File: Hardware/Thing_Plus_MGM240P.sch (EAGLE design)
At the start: 54 parts, among them J1 THING_PLUS_LOGICAL, J2 USB Female Type C Connector, J3 QWIIC_RIGHT_ANGLE, J5 MICRO-SDFRICTION, Q1 20V/4.2A/52mΩ/1.4W, U1 MGM240P, U2 3.3V, U4 MCP73831, U5 MAX17048, U6 MK22FN128VLH10

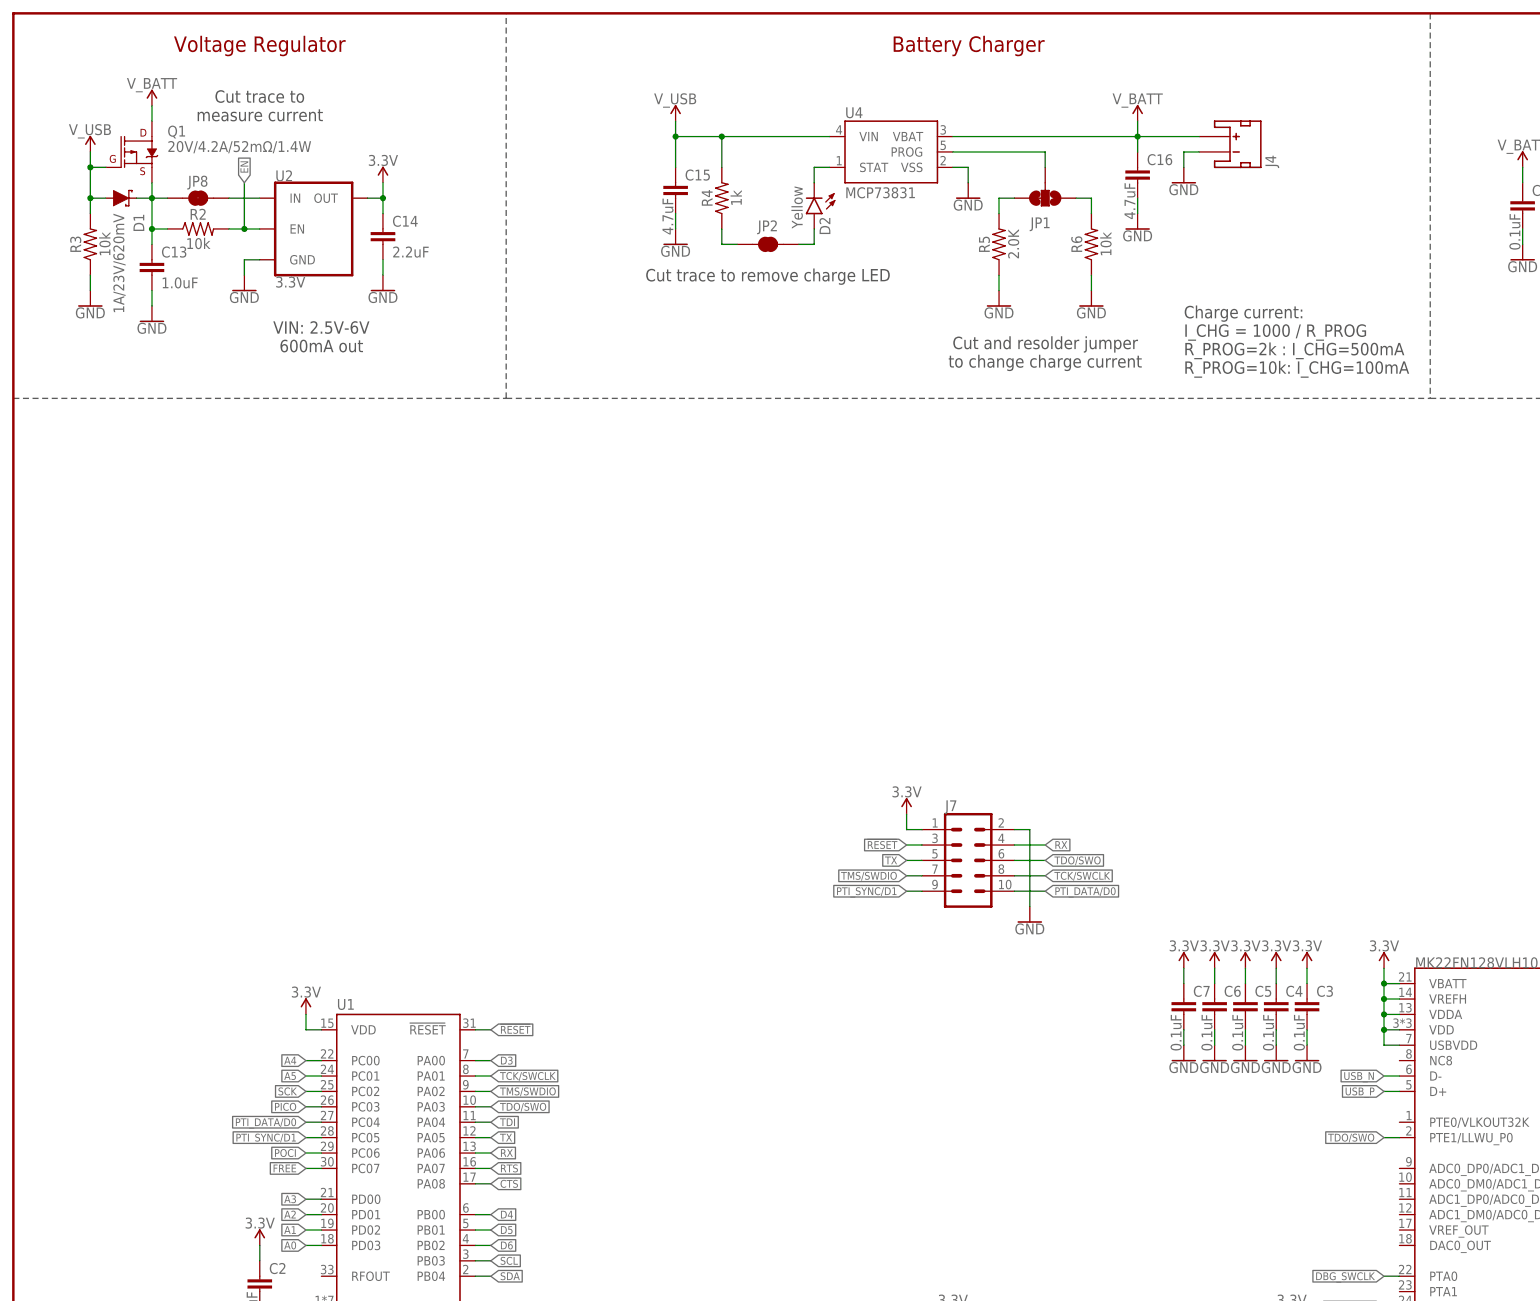
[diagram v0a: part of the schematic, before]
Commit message: Schematic and board updates
Disconnect RTS and CTS pins
Add status LED
Complete more of the routing and component placement
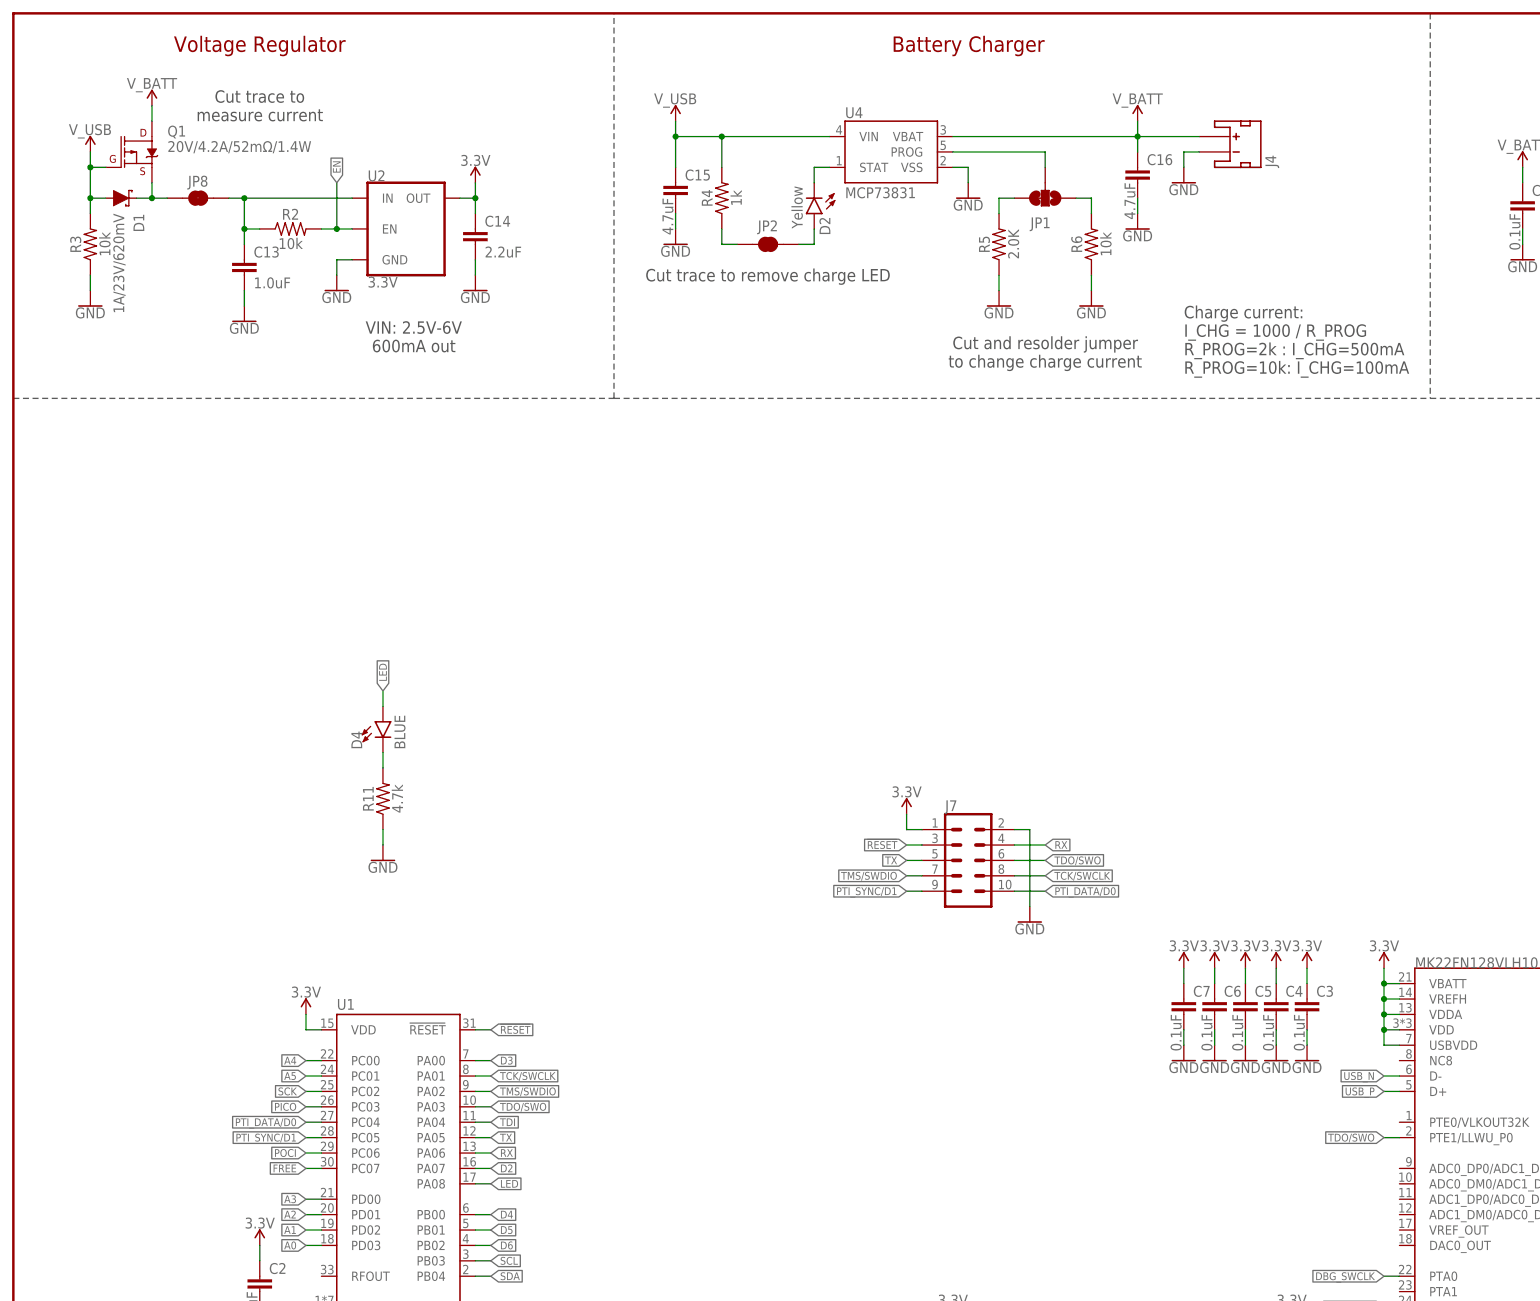
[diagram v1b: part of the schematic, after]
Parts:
- added D4: BLUE, SparkFun-LED:LED-BLUE0603
- added R11: 4.7k, SparkFun-Resistors:4.7KOHM-0402T-1/16W-1%
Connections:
- removed net N$2: C13.1, D1.C, JP8.1, Q1.S, R2.1
- new net LED: D4.A, U1.PA08
- new net N$1: D4.C, R11.2
- new net N$7: D1.C, JP8.1, Q1.S
- net CTS: no longer U1.PA08
- net D2: now also U1.PA07
- net GND: now also R11.1
- net N$27: now also C13.1, R2.1
- net RTS: no longer U1.PA07
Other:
- moved on the sheet: C13, C14, R2, U2

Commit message: Finalize initial schematic and board
Clean up schematic and finalize nets
Finish routing board (needs improved GND continuity
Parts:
- added LOGO1: SFE_LOGO_NAME_FLAME.1_INCH, SparkFun-Aesthetics:SFE_LOGO_NAME_FLAME.1_INCH
- added LOGO2: QWIIC_LOGO_3MM, SparkFun-Aesthetics:QWIIC_LOGO_3MM
- added LOGO3: OSHW-LOGOS, SparkFun-Aesthetics:OSHW-LOGOS
- added Q2: 20V/4.2A/52mΩ/1.4W, SparkFun-DiscreteSemi:MOSFET_PCH-DMG2305UX-7
- added R12: 100k, SparkFun-Resistors:100KOHM-0402T-1/16W-1%
- added VDDJ_EN: JUMPER-SMT_2_NO_SILK, SparkFun-Jumpers:JUMPER-SMT_2_NO_SILK
- renumbered JP2 to CHG, JP3 to I2C, JP4 to SHLD, JP8 to MEAS
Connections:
- removed net SCL1: U5.SCL
- removed net SDA1: U5.SDA
- new net !VDDJ_EN!: Q2.G, R12.2, VDDJ_EN.2
- new net VDD: C3.1, C4.1, C5.1, C6.1, C7.1, Q2.D, R1.2, TP1.1, U6.PTA4/LLWU_P3, U6.USBVDD, U6.VBATT, U6.VDD, U6.VDDA, U6.VREFH
- net 3.3V: now also Q2.S; no longer C3.1, C4.1, C5.1, C6.1, C7.1, R1.2, TP1.1, U6.PTA4/LLWU_P3, U6.USBVDD, U6.VBATT, U6.VDD, U6.VDDA, U6.VREFH
- net A0: now also VDDJ_EN.1
- net GND: now also R12.1
- net SCL: now also U5.SCL
- net SDA: now also U5.SDA
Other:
- note added: "Close jumper to enable power control of J-Link OB Debugger"
- note added: "Dryw Wade"
- note added: "J-Link 6 Pin Adapter Test Points"
- note added: "J-Link OB Debugger"
- note added: "J-Link OB Power Control"
- note added: "MGM240P"
- note added: "Mini Simplicity Connector"
- note added: "Status LED"
- note added: "Thing Plus Pinout"
- note added: "v01"
- moved on the sheet: C2, C3, C4, C5, C6, C7, D4, J1, J5, J7, R1, R11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

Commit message: Add polish
Improve GND continuity
Fix and approve DRC errors
Add SFE flame and OSHW logo to top silk
Add pin and jumper labels to bottom silk
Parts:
- renumbered JP1 to CHG_I, VDDJ_EN to VJ_CTRL
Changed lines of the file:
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@@
 <part name="R5" library="SparkFun-Resistors" deviceset="2.0KOHM" device="-0402T-1/16W-1%" value="2.0K"/>
 <part name="R6" library="SparkFun-Resistors" deviceset="10KOHM" device="-0402T-1/16W-1%" value="10k"/>
-<part name="JP1" library="SparkFun-Jumpers" deviceset="JUMPER-SMT_3_1-NC_TRACE" device="_SILK" package3d_urn="urn:adsk.eagle:package:39288/1"/>
+<part name="CHG_I" library="SparkFun-Jumpers" deviceset="JUMPER-SMT_3_1-NC_TRACE" device="_SILK" package3d_urn="urn:adsk.eagle:package:39288/1"/>
 <part name="GND29" library="SparkFun-PowerSymbols" deviceset="GND" device=""/>
 <part name="GND30" library="SparkFun-PowerSymbols" deviceset="GND" device=""/>
@@
 <part name="R12" library="SparkFun-Resistors" deviceset="100KOHM" device="-0402T-1/16W-1%" value="100k"/>
 <part name="GND18" library="SparkFun-PowerSymbols" deviceset="GND" device=""/>
-<part name="VDDJ_EN" library="SparkFun-Jumpers" deviceset="JUMPER-SMT_2_NO" device="_SILK" package3d_urn="urn:adsk.eagle:package:39279/1"/>
+<part name="VJ_CTRL" library="SparkFun-Jumpers" deviceset="JUMPER-SMT_2_NO" device="_SILK" package3d_urn="urn:adsk.eagle:package:39279/1"/>
 <part name="LOGO1" library="SparkFun-Aesthetics" deviceset="SFE_LOGO_NAME_FLAME" device=".1_INCH"/>
 <part name="LOGO2" library="SparkFun-Aesthetics" deviceset="QWIIC_LOGO" device="_3MM"/>
@@
 <attribute name="VALUE" x="179.324" y="241.3" size="1.778" layer="96" font="vector" rot="R90" align="top-center"/>
 </instance>
-<instance part="JP1" gate="G$1" x="170.18" y="248.92" smashed="yes" rot="R270">
+<instance part="CHG_I" gate="G$1" x="170.18" y="248.92" smashed="yes" rot="R270">
 <attribute name="NAME" x="169.418" y="244.856" size="1.778" layer="95" font="vector" rot="R180" align="center"/>
 </instance>
@@
 <attribute name="VALUE" x="297.18" y="169.926" size="1.778" layer="96" align="top-center"/>
 </instance>
-<instance part="VDDJ_EN" gate="G$1" x="297.18" y="162.56" smashed="yes">
+<instance part="VJ_CTRL" gate="G$1" x="297.18" y="162.56" smashed="yes">
 <attribute name="NAME" x="297.18" y="165.354" size="1.778" layer="95" font="vector" align="center"/>
 </instance>
@@
 <pinref part="R6" gate="G$1" pin="2"/>
 <wire x1="177.8" y1="246.38" x2="177.8" y2="248.92" width="0.1524" layer="91"/>
-<pinref part="JP1" gate="G$1" pin="1"/>
+<pinref part="CHG_I" gate="G$1" pin="1"/>
 <wire x1="177.8" y1="248.92" x2="175.26" y2="248.92" width="0.1524" layer="91"/>
 </segment>
@@
 <pinref part="R5" gate="G$1" pin="2"/>
 <wire x1="162.56" y1="246.38" x2="162.56" y2="248.92" width="0.1524" layer="91"/>
-<pinref part="JP1" gate="G$1" pin="3"/>
+<pinref part="CHG_I" gate="G$1" pin="3"/>
 <wire x1="162.56" y1="248.92" x2="165.1" y2="248.92" width="0.1524" layer="91"/>
 </segment>
@@
 <net name="N$9" class="0">
 <segment>
-<pinref part="JP1" gate="G$1" pin="2"/>
+<pinref part="CHG_I" gate="G$1" pin="2"/>
 <wire x1="170.18" y1="254" x2="170.18" y2="256.54" width="0.1524" layer="91"/>
 <pinref part="U4" gate="G$1" pin="PROG"/>
@@
 </segment>
 <segment>
-<pinref part="VDDJ_EN" gate="G$1" pin="1"/>
+<pinref part="VJ_CTRL" gate="G$1" pin="1"/>
 <wire x1="292.1" y1="162.56" x2="289.56" y2="162.56" width="0.1524" layer="91" style="longdash"/>
 <label x="289.56" y="162.56" size="1.27" layer="95" rot="R180" xref="yes"/>
@@
 </segment>
 <segment>
-<pinref part="VDDJ_EN" gate="G$1" pin="2"/>
+<pinref part="VJ_CTRL" gate="G$1" pin="2"/>
 <wire x1="302.26" y1="162.56" x2="304.8" y2="162.56" width="0.1524" layer="91" style="longdash"/>
 <label x="304.8" y="162.56" size="1.27" layer="95" xref="yes"/>

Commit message: Update voltage regulator
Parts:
- U2: value 3.3V -> XC6222B331MR-G; device SparkFun-IC-Power:V_REG_AP2112K-3.3V -> SparkFun-IC-Power:XC6222B331MR-G
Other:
- note added: "VIN: 2.5V-6V 700mA out"
- note removed: "VIN: 2.5V-6V 600mA out"
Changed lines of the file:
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@@
 <part name="GND5" library="SparkFun-PowerSymbols" deviceset="GND" device=""/>
 <part name="SUPPLY8" library="SparkFun-PowerSymbols" deviceset="V_BATT" device=""/>
-<part name="U2" library="SparkFun-IC-Power" deviceset="V_REG_AP2112" device="K-3.3V" value="3.3V"/>
+<part name="U2" library="SparkFun-IC-Power" deviceset="XC6222" device="B331MR-G" value="XC6222B331MR-G"/>
 <part name="SUPPLY9" library="SparkFun-PowerSymbols" deviceset="3.3V" device=""/>
 <part name="GND6" library="SparkFun-PowerSymbols" deviceset="GND" device=""/>
@@
 to change charge current</text>
 <text x="66.04" y="226.06" size="2.032" layer="97" font="vector" align="center">VIN: 2.5V-6V
-600mA out</text>
+700mA out</text>
 <text x="335.28" y="228.6" size="2.032" layer="97" font="vector" align="center">Cut trace to isolate
 shield from GND</text>
@@
 <instance part="U2" gate="G$1" x="66.04" y="243.84" smashed="yes">
 <attribute name="NAME" x="58.42" y="251.714" size="1.778" layer="95" font="vector"/>
-<attribute name="VALUE" x="58.42" y="235.966" size="1.778" layer="96" font="vector" align="top-left"/>
 </instance>
 <instance part="SUPPLY9" gate="G$1" x="76.2" y="251.46" smashed="yes">

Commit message: Design review updates
Add reset button
Add power LED
Pour USB shield on bottom too
Increase VUSB trace to 20mil
Add silk labels for LEDs
Add version number to copper
Change charge LED resistor value
Add "Thing Plus" to bottom silk
Add measures
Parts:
- added D5: RED, SparkFun-LED:LED-RED0603
- added PWR: JUMPER-SMT_2_NC_TRACE_SILK, SparkFun-Jumpers:JUMPER-SMT_2_NC_TRACE_SILK
- added R13: 1k, SparkFun-Resistors:1KOHM-0402T-1/16W-1%
- added S1: MOMENTARY-SWITCH-SPST-SMD-4.6X2.8MM, SparkFun-Switches:MOMENTARY-SWITCH-SPST-SMD-4.6X2.8MM
- R4: value 1k -> 4.7k; device SparkFun-Resistors:1KOHM-0402T-1/16W-1% -> SparkFun-Resistors:4.7KOHM-0402T-1/16W-1%
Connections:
- new net N$2: PWR.1, R13.2
- new net N$8: D5.A, R13.1
- net !RESET!: now also S1.2
- net 3.3V: now also PWR.2
- net GND: now also D5.C, S1.1
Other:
- note added: "Cut trace to remove power LED"
- note added: "Power LED"
- note added: "Reset Button"
- note added: "Voltage Range: 1.8V to 3.8V"
- moved on the sheet: J5

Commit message: Design review updates
Chang USB connector to 2-layer version
Fix gague typo in schematic
Remove UART flow control nets from J-Link
Spread out J-Link caps in schematic
Remove right angles from VDDJ trace and straighten out
Fix acid trap
Move reset button and 2 caps away from J-Link chip
Move POCI to top layer at SD card
Fix USB width before ESD protection
Thicker USB ESD trace
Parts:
- J2: device SparkFun-Connectors:USB_C_4-LAYER-ISOLATED -> SparkFun-Connectors:USB_C_2-LAYER_PADS
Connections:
- removed net CTS: U6.PTB3
- removed net RTS: U6.PTB2
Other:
- note added: "Battery Fuel Gauge"
- note removed: "Battery Fuel Gague"
- moved on the sheet: C3, C4, C5, C6, C7

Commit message: Design review updates
Change to 4-layer board for better EMC and routing
Remove excessive GND vias now that it's 4 layers
Add label to reset button in silk
Add 10uF cap for SD card
Change net names to represent MGM240P port names rather than Arduino names
Connect uSD CS pin to PA07
Fix acid traps
Reposition MEAS to be off-grid to prevent confusion
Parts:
- added C1: 10uF, SparkFun-Capacitors:10UF-0402T-6.3V-20%
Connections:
- net A0 renamed PD03
- net A1 renamed PD02
- net A2 renamed PD01
- net A3 renamed PD00
- net A4 renamed PC00
- net A5 renamed PC01
- net D3 renamed PA00
- net D4 renamed PB00
- net D5 renamed PB01
- net D6 renamed PB02
- net FREE renamed PC07
- net LED renamed LED/PA08
- net PICO renamed PICO/PC03
- net POCI renamed POCI/PC06
- net PTI_DATA/D0 renamed PTI_DATA/PC04
- net PTI_SYNC/D1 renamed PTI_SYNC/PC05
- net RX renamed RX/PA06
- net SCK renamed SCK/PC02
- net SCL renamed SCL/PB03
- net SDA renamed SDA/PB04
- net TCK/SWCLK renamed TCK/SWCLK/PA01
- net TDI renamed TDI/PA04
- net TDO/SWO renamed TDO/SWO/PA03
- net TMS/SWDIO renamed TMS/SWDIO/PA02
- net TX renamed TX/PA05
- removed net D2: J1.GPIO2, U1.PA07
- removed net N$37: J5.DAT3/!CS!
- new net PA07: J1.GPIO2, J5.DAT3/!CS!, U1.PA07
- net 3.3V: now also C1.1
- net GND: now also C1.2
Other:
- moved on the sheet: D4, D5, J5, J7, PWR, Q2, R11, R12, R13, S1, TP1, TP2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
